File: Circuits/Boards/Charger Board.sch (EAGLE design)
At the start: 62 parts, among them CON1 ISP(2X3), CON10 HEADER_3X1, CON11 HEADER_3X1, CON12 HEADER_3X1, CON3 HEADER_3X1, CON4 HEADER_3X1, CON5 HEADER_3X1, CON6 HEADER_3X1, CON7 HEADER_3X1, CON8 HEADER_3X1, CON9 HEADER_3X1, IC1 NCP1117DT33G, T1 NPN2N2222, T2 NPN2N2222, T3 SI4421DY, U1 ATMEGA324P, U2 ACS711

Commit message: updates to both boards
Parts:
- removed C2: 1nf, Passive:CAP0603
- removed R1: 1k, Passive:RES0603
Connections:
- removed net N$12: C2.1, R1.1, U2.VIOUT
- removed net N$25: C4.1, IC1.IN, S1.2
- new net VIN: S1.1
- net +5V: now also C4.1, IC1.IN, S1.2; no longer S1.1
- net CURRENTSENSE: now also U2.VIOUT; no longer R1.2
- net GND: no longer C2.2
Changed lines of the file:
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@@
 <part name="C1" library="Passive" deviceset="CAP" device="0603" value=".1uf"/>
 <part name="GND3" library="Supply" deviceset="GND" device=""/>
-<part name="C2" library="Passive" deviceset="CAP" device="0603" value="1nf"/>
-<part name="GND7" library="Supply" deviceset="GND" device=""/>
-<part name="R1" library="Passive" deviceset="RES" device="0603" value="1k"/>
 <part name="P+4" library="Supply" deviceset="+5V" device=""/>
 <part name="P+8" library="Supply" deviceset="+5V" device=""/>
@@
 <instance part="C1" gate="G$1" x="17.78" y="-88.9"/>
 <instance part="GND3" gate="1" x="17.78" y="-96.52"/>
-<instance part="C2" gate="G$1" x="22.86" y="-109.22"/>
-<instance part="GND7" gate="1" x="22.86" y="-116.84"/>
-<instance part="R1" gate="G$1" x="33.02" y="-101.6"/>
-<instance part="P+4" gate="1" x="-43.18" y="109.22"/>
+<instance part="P+4" gate="1" x="-12.7" y="106.68"/>
 <instance part="P+8" gate="1" x="-58.42" y="-63.5"/>
 <instance part="GND9" gate="1" x="5.08" y="83.82"/>
@@
 </segment>
 <segment>
-<pinref part="C2" gate="G$1" pin="2"/>
-<pinref part="GND7" gate="1" pin="GND"/>
-<wire x1="22.86" y1="-114.3" x2="22.86" y2="-111.76" width="0.1524" layer="91"/>
-</segment>
-<segment>
 <pinref part="CON3" gate="G$1" pin="3"/>
 <wire x1="175.26" y1="-99.06" x2="175.26" y2="-104.14" width="0.1524" layer="91"/>
@@
 </segment>
 <segment>
-<pinref part="S1" gate="G$1" pin="1"/>
-<wire x1="-33.02" y1="101.6" x2="-43.18" y2="101.6" width="0.1524" layer="91"/>
+<pinref part="S1" gate="G$1" pin="2"/>
+<pinref part="IC1" gate="G$1" pin="IN"/>
+<wire x1="-20.32" y1="101.6" x2="-12.7" y2="101.6" width="0.1524" layer="91"/>
+<pinref part="C4" gate="G$1" pin="1"/>
+<wire x1="-12.7" y1="101.6" x2="-7.62" y2="101.6" width="0.1524" layer="91"/>
+<wire x1="-12.7" y1="101.6" x2="-12.7" y2="99.06" width="0.1524" layer="91"/>
+<junction x="-12.7" y="101.6"/>
 <pinref part="P+4" gate="1" pin="+5V"/>
-<wire x1="-43.18" y1="101.6" x2="-43.18" y2="106.68" width="0.1524" layer="91"/>
+<wire x1="-12.7" y1="101.6" x2="-12.7" y2="104.14" width="0.1524" layer="91"/>
 </segment>
 </net>
@@
 </segment>
 <segment>
-<pinref part="R1" gate="G$1" pin="2"/>
-<wire x1="38.1" y1="-101.6" x2="43.18" y2="-101.6" width="0.1524" layer="91"/>
-<label x="43.18" y="-101.6" size="1.778" layer="91" xref="yes"/>
+<pinref part="U2" gate="G$1" pin="VIOUT"/>
+<wire x1="7.62" y1="-101.6" x2="27.94" y2="-101.6" width="0.1524" layer="91"/>
+<label x="27.94" y="-101.6" size="1.778" layer="91" xref="yes"/>
 </segment>
 </net>
@@
 <wire x1="-58.42" y1="-83.82" x2="-58.42" y2="-88.9" width="0.1524" layer="91"/>
 <pinref part="T3" gate="G$1" pin="D"/>
-</segment>
-</net>
-<net name="N$12" class="0">
-<segment>
-<pinref part="U2" gate="G$1" pin="VIOUT"/>
-<pinref part="R1" gate="G$1" pin="1"/>
-<wire x1="7.62" y1="-101.6" x2="22.86" y2="-101.6" width="0.1524" layer="91"/>
-<pinref part="C2" gate="G$1" pin="1"/>
-<wire x1="22.86" y1="-101.6" x2="27.94" y2="-101.6" width="0.1524" layer="91"/>
-<wire x1="22.86" y1="-101.6" x2="22.86" y2="-104.14" width="0.1524" layer="91"/>
 </segment>
 </net>
@@
 </segment>
 </net>
-<net name="N$25" class="0">
-<segment>
-<pinref part="S1" gate="G$1" pin="2"/>
-<pinref part="IC1" gate="G$1" pin="IN"/>
-<wire x1="-20.32" y1="101.6" x2="-12.7" y2="101.6" width="0.1524" layer="91"/>
-<pinref part="C4" gate="G$1" pin="1"/>
-<wire x1="-12.7" y1="101.6" x2="-7.62" y2="101.6" width="0.1524" layer="91"/>
-<wire x1="-12.7" y1="101.6" x2="-12.7" y2="99.06" width="0.1524" layer="91"/>
-<junction x="-12.7" y="101.6"/>
-</segment>
-</net>
 <net name="SECTION2" class="0">
 <segment>
@@
 </segment>
 </net>
+<net name="VIN" class="0">
+<segment>
+<pinref part="S1" gate="G$1" pin="1"/>
+<wire x1="-33.02" y1="101.6" x2="-66.04" y2="101.6" width="0.1524" layer="91"/>
+<label x="-58.42" y="101.6" size="1.778" layer="91"/>
+</segment>
+</net>

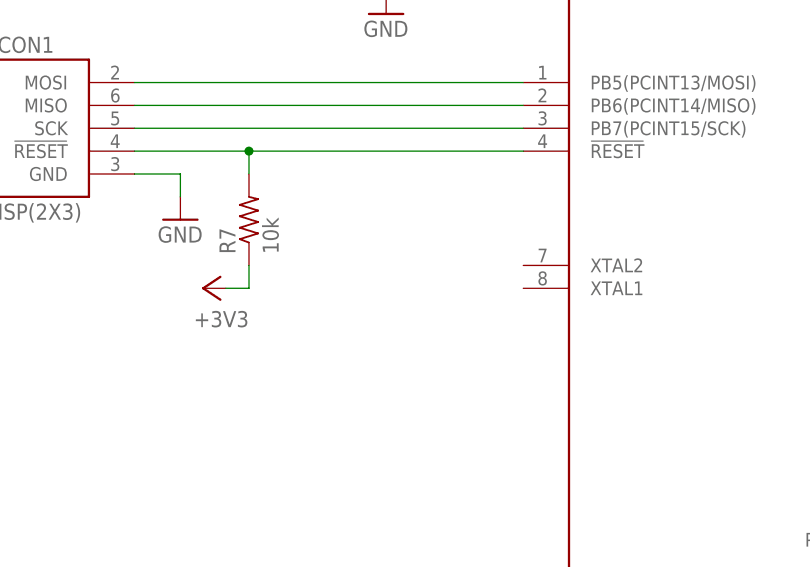
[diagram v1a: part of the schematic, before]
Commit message: 
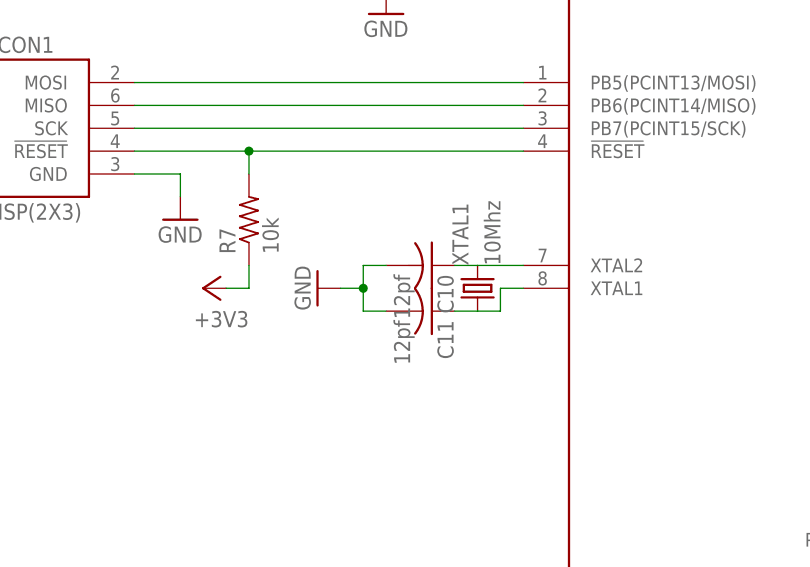
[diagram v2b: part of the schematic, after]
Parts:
- added C10, C11: 12pf, Passive:CAP0603
- added XTAL1: 10Mhz, Passive:NX5032GA-10.000000MHZ
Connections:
- new net N$12: C10.1, XTAL1.2
- new net N$25: C11.1, XTAL1.1
- net GND: now also C10.2, C11.2
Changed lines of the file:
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@@
 <part name="U$3" library="Passive" deviceset="MBRS410LT3" device=""/>
 <part name="U$4" library="Passive" deviceset="MBRS410LT3" device=""/>
+<part name="XTAL1" library="Passive" deviceset="NX5032GA-10.000000MHZ" device="" value="10Mhz"/>
+<part name="C10" library="Passive" deviceset="CAP" device="0603" value="12pf"/>
+<part name="C11" library="Passive" deviceset="CAP" device="0603" value="12pf"/>
+<part name="GND27" library="Supply" deviceset="GND" device=""/>
 </parts>
 <sheets>
@@
 <instance part="U$3" gate="G$1" x="0" y="-121.92"/>
 <instance part="U$4" gate="G$1" x="0" y="-127"/>
+<instance part="XTAL1" gate="G$1" x="-38.1" y="-5.08" rot="R90"/>
+<instance part="C10" gate="G$1" x="-45.72" y="-2.54" rot="R270"/>
+<instance part="C11" gate="G$1" x="-45.72" y="-7.62" rot="R270"/>
+<instance part="GND27" gate="1" x="-55.88" y="-5.08" rot="R270"/>
 </instances>
 <busses>
@@
 <junction x="5.08" y="88.9"/>
 </segment>
+<segment>
+<pinref part="C10" gate="G$1" pin="2"/>
+<wire x1="-48.26" y1="-2.54" x2="-50.8" y2="-2.54" width="0.1524" layer="91"/>
+<wire x1="-50.8" y1="-2.54" x2="-50.8" y2="-5.08" width="0.1524" layer="91"/>
+<pinref part="C11" gate="G$1" pin="2"/>
+<wire x1="-50.8" y1="-5.08" x2="-50.8" y2="-7.62" width="0.1524" layer="91"/>
+<wire x1="-48.26" y1="-7.62" x2="-50.8" y2="-7.62" width="0.1524" layer="91"/>
+<wire x1="-50.8" y1="-5.08" x2="-53.34" y2="-5.08" width="0.1524" layer="91"/>
+<pinref part="GND27" gate="1" pin="GND"/>
+<junction x="-50.8" y="-5.08"/>
+</segment>
 </net>
 <net name="N$2" class="0">
@@
 </segment>
 </net>
+<net name="N$12" class="0">
+<segment>
+<pinref part="XTAL1" gate="G$1" pin="2"/>
+<wire x1="-33.02" y1="-2.54" x2="-38.1" y2="-2.54" width="0.1524" layer="91"/>
+<wire x1="-38.1" y1="-2.54" x2="-40.64" y2="-2.54" width="0.1524" layer="91"/>
+<pinref part="C10" gate="G$1" pin="1"/>
+</segment>
+</net>
+<net name="N$25" class="0">
+<segment>
+<wire x1="-33.02" y1="-5.08" x2="-35.56" y2="-5.08" width="0.1524" layer="91"/>
+<pinref part="XTAL1" gate="G$1" pin="1"/>
+<wire x1="-35.56" y1="-5.08" x2="-35.56" y2="-7.62" width="0.1524" layer="91"/>
+<wire x1="-35.56" y1="-7.62" x2="-38.1" y2="-7.62" width="0.1524" layer="91"/>
+<wire x1="-38.1" y1="-7.62" x2="-40.64" y2="-7.62" width="0.1524" layer="91"/>
+<pinref part="C11" gate="G$1" pin="1"/>
+</segment>
+</net>

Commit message: 
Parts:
- added H1, H2, H3, H4: MOUNTINGHOLE, Mechanical:MOUNTINGHOLE
- R27: value 200 -> 470
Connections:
- removed net LED3: R27.1, U1.PB3(AIN1/OC0A/PCINT11)
- removed net N$39: CON6.1, R5.2
- removed net N$40: CON7.1, R6.2
- removed net N$41: CON8.1, R9.2
- removed net N$42: CON9.1, R17.2
- removed net N$43: CON10.1, R18.2
- removed net N$44: CON11.1, R19.2
- removed net N$45: CON12.1, R20.2
- new net N$30: CON7.3, R6.2
- new net N$31: CON8.3, R9.2
- new net N$32: CON9.3, R17.2
- new net N$33: CON10.3, R18.2
- new net N$34: CON11.3, R19.2
- new net N$35: CON12.3, R20.2
- net +3V3: no longer LED9.A
- net BUZZER: now also U1.PB4(!SS!/OC0B/PCINT12)
- net GND: now also CON10.1, CON11.1, CON12.1, CON3.1, CON4.1, CON5.1, CON6.1, CON7.1, CON8.1, CON9.1, R25.1, R26.1, R27.1; no longer CON10.3, CON11.3, CON12.3, CON3.3, CON4.3, CON5.3, CON6.3, CON7.3, CON8.3, CON9.3
- net LED1: now also LED9.A; no longer R25.1
- net LED2: now also LED8.A; no longer R26.1
- net N$1: now also LED10.A
- net N$12: now also U1.XTAL2
- net N$24: now also CON3.3, R2.2; no longer LED10.A, LED8.A
- net N$25: now also U1.XTAL1
- net N$27: now also CON4.3, R3.2; no longer CON3.1, R2.2
- net N$28: now also CON5.3, R4.2; no longer CON4.1, R3.2
- net N$29: now also CON6.3, R5.2; no longer CON5.1, R4.2
- net SECTION1: now also U1.PD4(PCINT28/XCK1/OC1B)
- net SECTION10: now also U1.PC5(TDI/PCINT21)
- net SECTION2: now also U1.PD5(PCINT29/OC1A)
- net SECTION3: now also U1.PD6(PCINT30/OC2B/ICP)
- net SECTION4: now also U1.PD7(PCINT31/OC2A)
- net SECTION5: now also U1.PC0(PCINT16/SCL)
- net SECTION6: now also U1.PC1(PCINT17/SDA)
- net SECTION7: now also U1.PC2(PCINT18/TCK)
- net SECTION8: now also U1.PC3(PCINT19/TMS)
- net SECTION9: now also U1.PC4(TDO/PCINT20)
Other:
- moved on the sheet: LED10, R17, R18, R19, R2, R20, R27, R3, R4, R5, R6, R9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

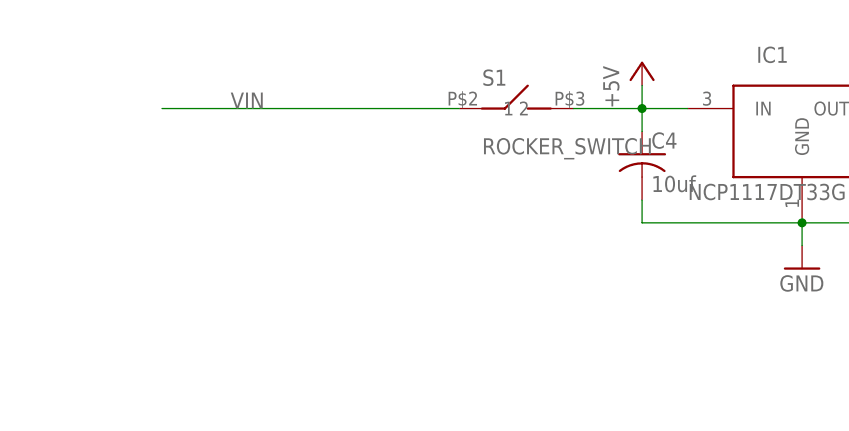
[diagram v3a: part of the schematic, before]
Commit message: 
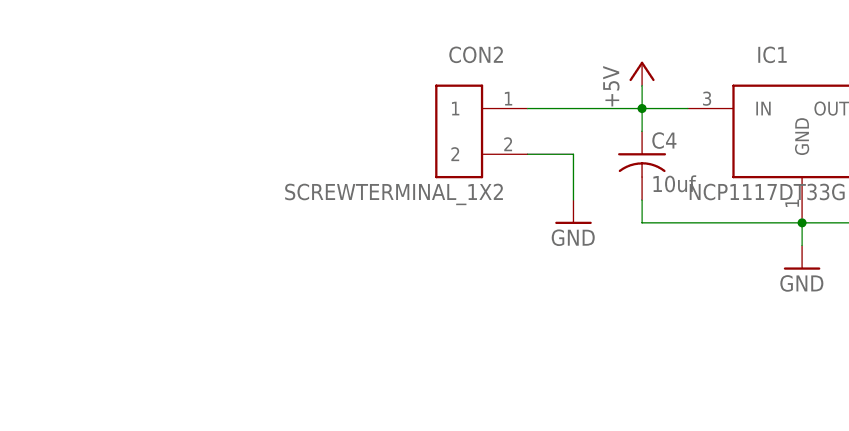
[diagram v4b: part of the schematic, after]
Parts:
- removed S1: ROCKER_SWITCH, Mechanical:ROCKER_SWITCH
- added CON2: SCREWTERMINAL_1X2, Mechanical:SCREWTERMINAL_1X2
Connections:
- removed net VIN: S1.1
- net +5V: now also CON2.1; no longer S1.2
- net GND: now also CON2.2
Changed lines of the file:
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@@
 <part name="R27" library="Passive" deviceset="RES" device="0603" value="470"/>
 <part name="R28" library="Passive" deviceset="RES" device="0603"/>
-<part name="S1" library="Mechanical" deviceset="ROCKER_SWITCH" device=""/>
 <part name="U2" library="PowerIC" deviceset="ACS711" device=""/>
 <part name="C1" library="Passive" deviceset="CAP" device="0603" value=".1uf"/>
@@
 <part name="H4" library="Mechanical" deviceset="MOUNTINGHOLE" device=""/>
 <part name="GND11" library="Supply" deviceset="GND" device=""/>
+<part name="CON2" library="Mechanical" deviceset="SCREWTERMINAL_1X2" device=""/>
+<part name="GND12" library="Supply" deviceset="GND" device=""/>
 </parts>
 <sheets>
@@
 <instance part="R27" gate="G$1" x="-50.8" y="-106.68" rot="R90"/>
 <instance part="R28" gate="G$1" x="-167.64" y="48.26"/>
-<instance part="S1" gate="G$1" x="-25.4" y="101.6"/>
 <instance part="U2" gate="G$1" x="-5.08" y="-93.98"/>
 <instance part="C1" gate="G$1" x="17.78" y="-88.9"/>
@@
 <instance part="H4" gate="G$1" x="-127" y="-53.34"/>
 <instance part="GND11" gate="1" x="-170.18" y="-27.94"/>
+<instance part="CON2" gate="G$1" x="-27.94" y="99.06" rot="MR0"/>
+<instance part="GND12" gate="1" x="-20.32" y="88.9"/>
 </instances>
 <busses>
@@
 <pinref part="GND11" gate="1" pin="GND"/>
 </segment>
+<segment>
+<pinref part="CON2" gate="G$1" pin="2"/>
+<wire x1="-25.4" y1="96.52" x2="-20.32" y2="96.52" width="0.1524" layer="91"/>
+<wire x1="-20.32" y1="96.52" x2="-20.32" y2="91.44" width="0.1524" layer="91"/>
+<pinref part="GND12" gate="1" pin="GND"/>
+</segment>
 </net>
 <net name="N$2" class="0">
@@
 </segment>
 <segment>
-<pinref part="S1" gate="G$1" pin="2"/>
 <pinref part="IC1" gate="G$1" pin="IN"/>
-<wire x1="-20.32" y1="101.6" x2="-12.7" y2="101.6" width="0.1524" layer="91"/>
 <pinref part="C4" gate="G$1" pin="1"/>
 <wire x1="-12.7" y1="101.6" x2="-7.62" y2="101.6" width="0.1524" layer="91"/>
@@
 <pinref part="P+4" gate="1" pin="+5V"/>
 <wire x1="-12.7" y1="101.6" x2="-12.7" y2="104.14" width="0.1524" layer="91"/>
+<pinref part="CON2" gate="G$1" pin="1"/>
+<wire x1="-12.7" y1="101.6" x2="-25.4" y2="101.6" width="0.1524" layer="91"/>
 </segment>
 </net>
@@
 </segment>
 </net>
-<net name="VIN" class="0">
-<segment>
-<pinref part="S1" gate="G$1" pin="1"/>
-<wire x1="-33.02" y1="101.6" x2="-66.04" y2="101.6" width="0.1524" layer="91"/>
-<label x="-58.42" y="101.6" size="1.778" layer="91"/>
-</segment>
-</net>
